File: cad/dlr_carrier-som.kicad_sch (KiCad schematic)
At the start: 5 parts, among them J5 CM4_J2

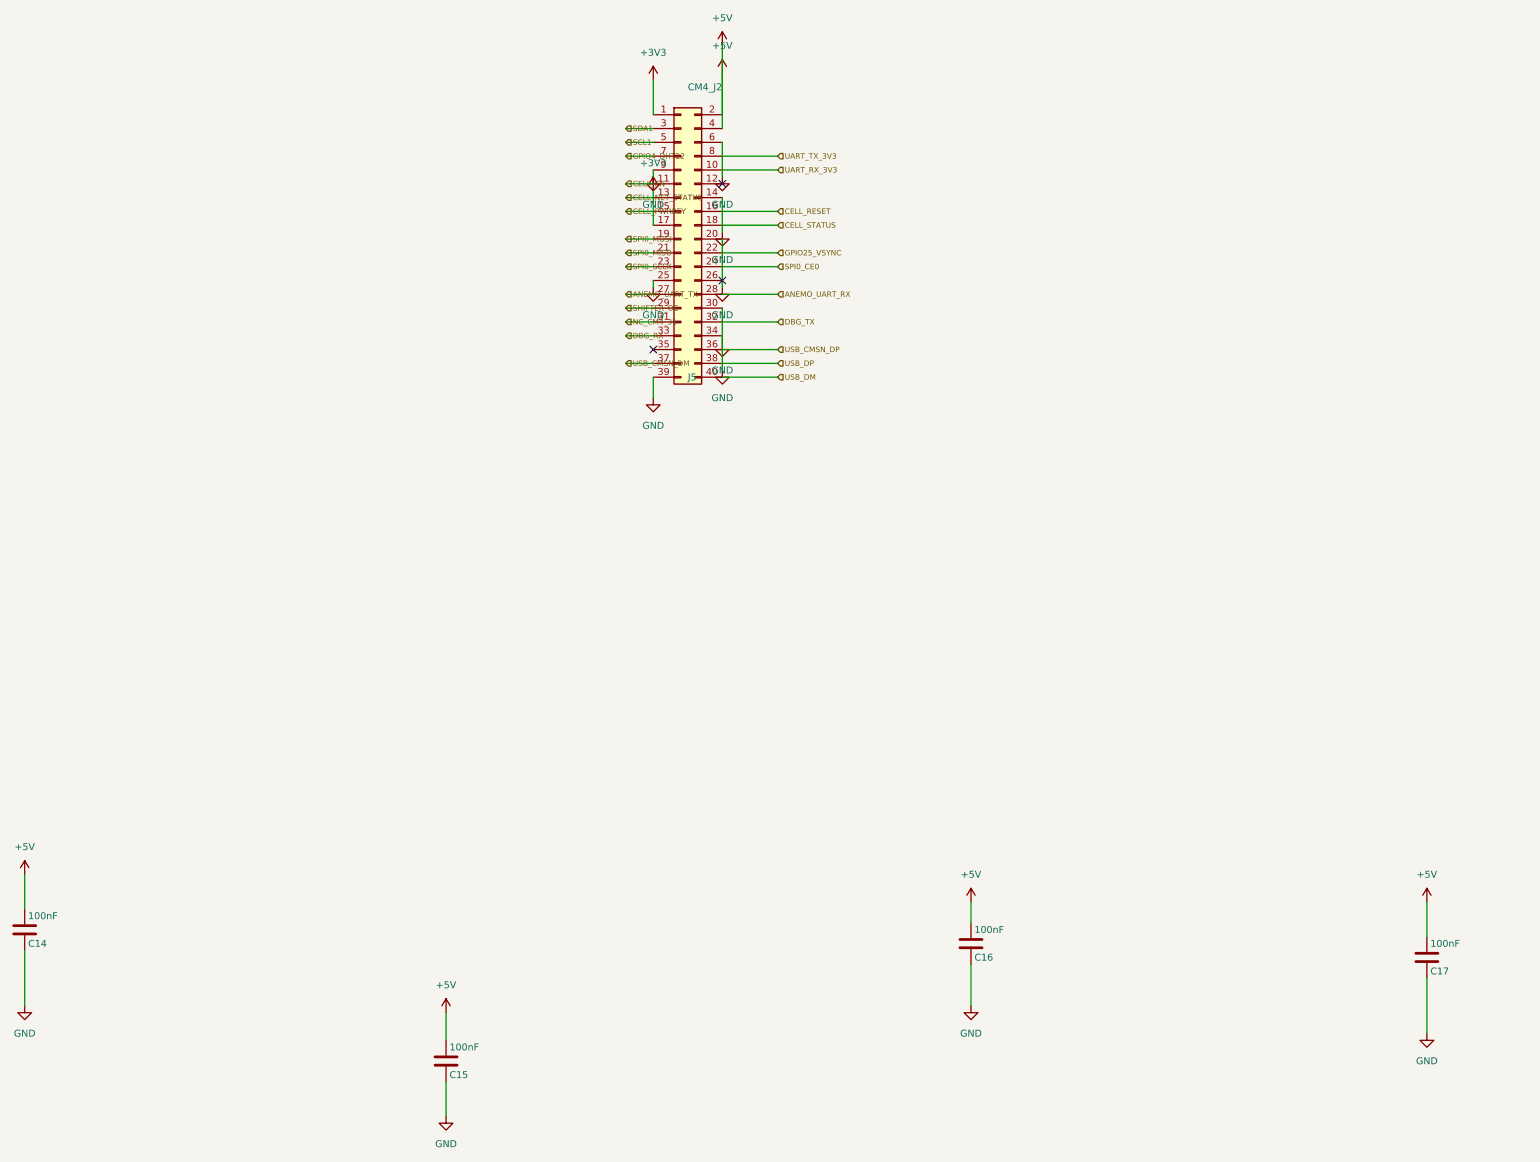
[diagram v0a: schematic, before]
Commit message: 🗺 feat(cad): scripted schematic + board pipeline, 4-layer stack
The committed board had almost every pad on +3V3 — no 5V_RAIL, VBAT or SDA1 net
existed on it at all — so the gerbers in output/ were never a valid board. Cause:
"Update PCB from Schematic" is GUI-only, so nothing kept the board honest, and the
schematic generator itself was merging nets.

Schematic generator:
  * power stubs now run along the pin direction; they used to be forced up or down
    regardless, which drove a 5V_RAIL stub straight through the buck inductor's
    BUCK_SW pin
  * PWR_FLAGs are placed by rule — any net that reaches a power-input pin with no
    power-output pin gets exactly one — instead of a hardcoded list, which is what
    the new VBAT and CHG_VCC rails needed
  * placement is deterministic; it used Python's salted hash(), so no two runs
    produced the same schematic
  * sch_guard fails the build on any cross-net wire/pin collision
  * ~700 lines of dead single-sheet generator removed
  ERC: 0 violations across all 8 sheets.

Board pipeline (cad/drawing/, all scripted, no GUI step):
  sync_pcb      rebuilds every footprint from the library and reassigns every pad
                net from the SKiDL netlist — the replacement for F8
  board_setup   4-layer SIG/GND/5V/SIG stack, rules, net classes, planes (ADR-016)
  route_pcb     DSN -> Freerouting -> SES, after patching the DSN so plane layers
                are "power" (the router was slicing the planes with signals) and
                the plane declarations are dropped (the router had been leaving
                GND and 5V pads with no path to the plane at all)
  stitch_planes vias from surface pads into their plane
  close_gaps    closes what the router leaves, using real segment-to-segment
                clearance; it never forces copper through another net

DRC: 265 unconnected -> 5, with no clearance, short, annular-ring or courtyard
errors. The remaining 5 are escapes on the DF40, the VQFN and the MSOP; they are
l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
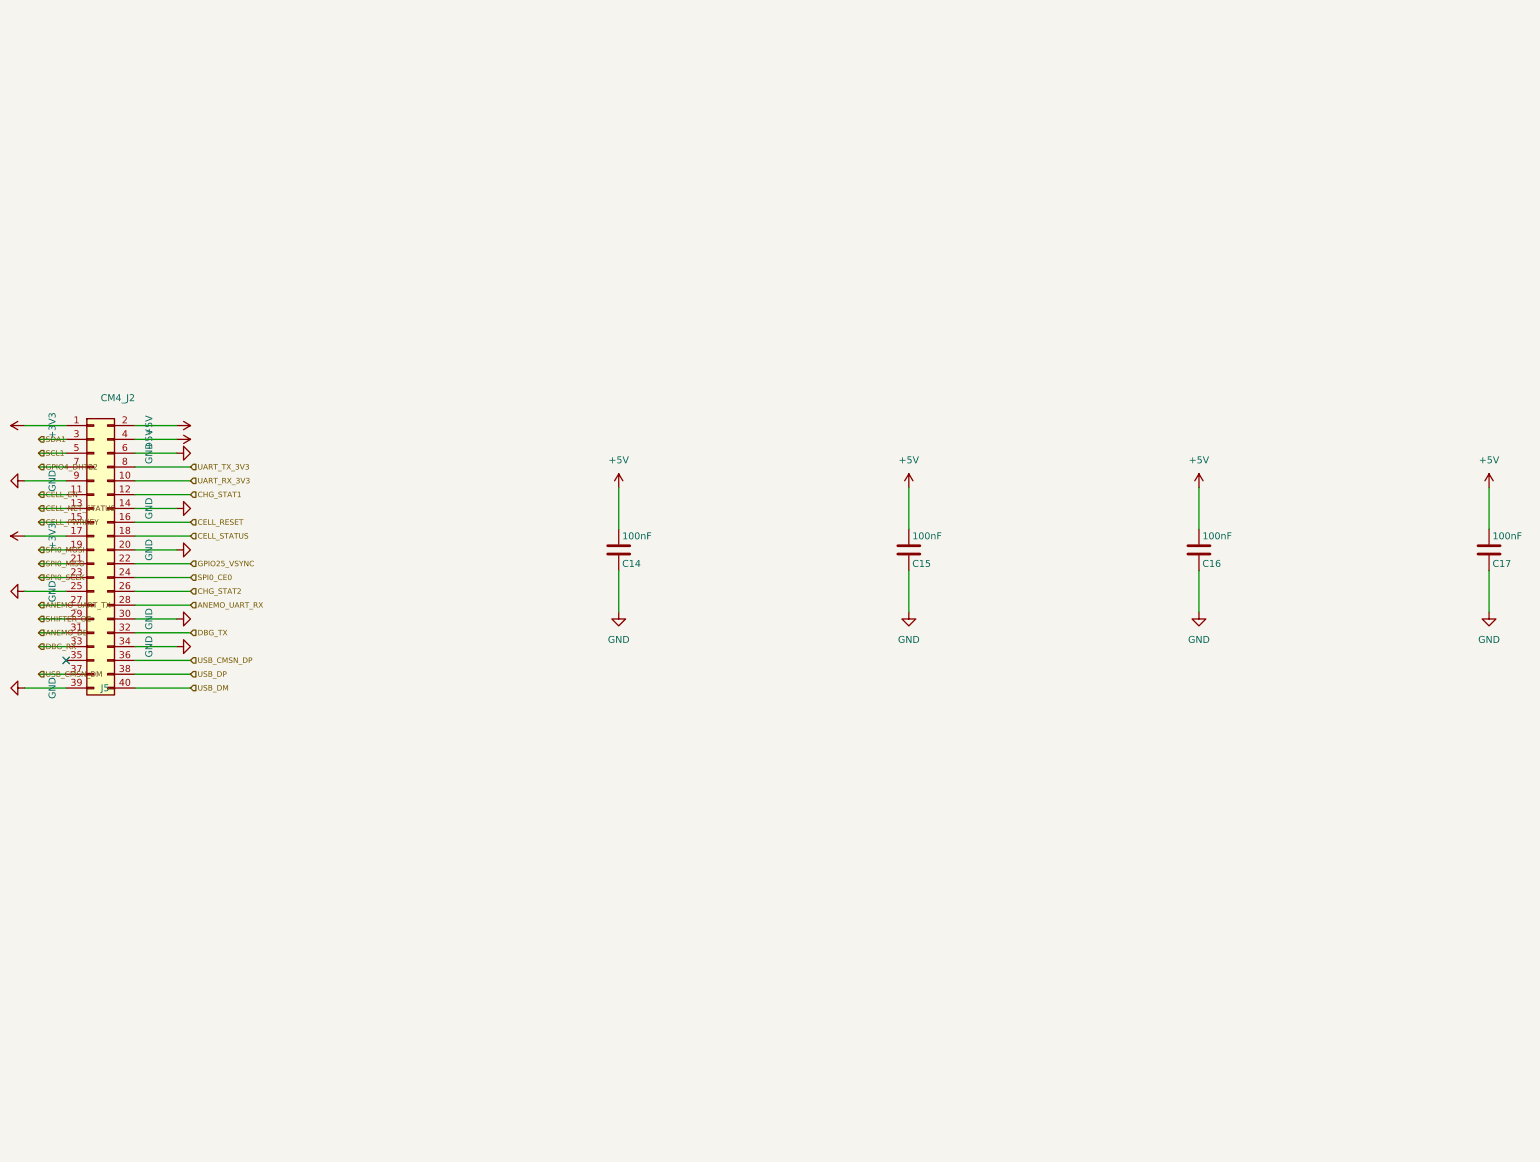
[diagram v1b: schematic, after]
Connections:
- net CHG_STAT1: now reaches J5.12 (Pin_12)
- net CHG_STAT2: now reaches J5.26 (Pin_26)
- net NC_CM4_31 renamed ANEMO_DE
- no-connect marks 3 -> 1

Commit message: 🩺 fix(schematic): match hierarchical label type to the sheet pin
The 117 KiCad 9 errors were a type mismatch, not the hierarchy metadata: every
child hierarchical label was written as `(shape input)` while the root's sheet pins
are bidirectional. KiCad's hier_label_mismatch check compares electrical type as
well as name, so on KiCad 9 every cross-sheet net failed, and the root labels then
read as dangling. KiCad 10 tolerates the mismatch, which is why it passed here.

kicad-sch-api 0.5.6 accepts a shape argument on add_hierarchical_label and ignores
it — the third serialization bug worked around in this generator — so the shape is
rewritten in the saved sheet.

Co-Authored-By: Claude Opus 5 <noreply@anthropic.com>
Claude-Session: https://claude.ai/code/session_011xr7VCL7rkJj2WE2uQF7sF
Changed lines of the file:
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@@
 		(instances
 			(project "CM4 SoM"
-				(path "/89720a6f-8597-4309-a3bf-d36a1edd93d6"
+				(path "/8bad8029-d445-45ba-bfa9-ecca933e2f0a"
 					(reference "J5")
 					(unit 1)
@@
 		(instances
 			(project "CM4 SoM"
-				(path "/89720a6f-8597-4309-a3bf-d36a1edd93d6"
+				(path "/8bad8029-d445-45ba-bfa9-ecca933e2f0a"
 					(reference "C14")
 					(unit 1)
@@
 		(instances
 			(project "CM4 SoM"
-				(path "/89720a6f-8597-4309-a3bf-d36a1edd93d6"
+				(path "/8bad8029-d445-45ba-bfa9-ecca933e2f0a"
 					(reference "C15")
 					(unit 1)
@@
 		(instances
 			(project "CM4 SoM"
-				(path "/89720a6f-8597-4309-a3bf-d36a1edd93d6"
+				(path "/8bad8029-d445-45ba-bfa9-ecca933e2f0a"
 					(reference "C16")
 					(unit 1)
@@
 		(instances
 			(project "CM4 SoM"
-				(path "/89720a6f-8597-4309-a3bf-d36a1edd93d6"
+				(path "/8bad8029-d445-45ba-bfa9-ecca933e2f0a"
 					(reference "C17")
 					(unit 1)
@@
 		(instances
 			(project "CM4 SoM"
-				(path "/89720a6f-8597-4309-a3bf-d36a1edd93d6"
+				(path "/8bad8029-d445-45ba-bfa9-ecca933e2f0a"
 					(reference "#PWR001")
 					(unit 1)
@@
 		(instances
 			(project "CM4 SoM"
-				(path "/89720a6f-8597-4309-a3bf-d36a1edd93d6"
+				(path "/8bad8029-d445-45ba-bfa9-ecca933e2f0a"
 					(reference "#PWR002")
 					(unit 1)
@@
 		(instances
 			(project "CM4 SoM"
-				(path "/89720a6f-8597-4309-a3bf-d36a1edd93d6"
+				(path "/8bad8029-d445-45ba-bfa9-ecca933e2f0a"
 					(reference "#PWR003")
 					(unit 1)
@@
 		(instances
 			(project "CM4 SoM"
-				(path "/89720a6f-8597-4309-a3bf-d36a1edd93d6"
+				(path "/8bad8029-d445-45ba-bfa9-ecca933e2f0a"
 					(reference "#PWR004")
 					(unit 1)
@@
 		(instances
 			(project "CM4 SoM"
-				(path "/89720a6f-8597-4309-a3bf-d36a1edd93d6"
+				(path "/8bad8029-d445-45ba-bfa9-ecca933e2f0a"
 					(reference "#PWR005")
 					(unit 1)
@@
 		(instances
 			(project "CM4 SoM"
-				(path "/89720a6f-8597-4309-a3bf-d36a1edd93d6"
+				(path "/8bad8029-d445-45ba-bfa9-ecca933e2f0a"
 					(reference "#PWR006")
 					(unit 1)
@@
 		(instances
 			(project "CM4 SoM"
-				(path "/89720a6f-8597-4309-a3bf-d36a1edd93d6"
+				(path "/8bad8029-d445-45ba-bfa9-ecca933e2f0a"
 					(reference "#PWR007")
 					(unit 1)
@@
 		(instances
 			(project "CM4 SoM"
-				(path "/89720a6f-8597-4309-a3bf-d36a1edd93d6"
+				(path "/8bad8029-d445-45ba-bfa9-ecca933e2f0a"
 					(reference "#PWR008")
 					(unit 1)
@@
 		(instances
 			(project "CM4 SoM"
-				(path "/89720a6f-8597-4309-a3bf-d36a1edd93d6"
+				(path "/8bad8029-d445-45ba-bfa9-ecca933e2f0a"
 					(reference "#PWR009")
 					(unit 1)
@@
 		(instances
 			(project "CM4 SoM"
-				(path "/89720a6f-8597-4309-a3bf-d36a1edd93d6"
+				(path "/8bad8029-d445-45ba-bfa9-ecca933e2f0a"
 					(reference "#PWR010")
 					(unit 1)
@@
 		(instances
 			(project "CM4 SoM"
-				(path "/89720a6f-8597-4309-a3bf-d36a1edd93d6"
+				(path "/8bad8029-d445-45ba-bfa9-ecca933e2f0a"
 					(reference "#PWR011")
 					(unit 1)
@@
 		(instances
 			(project "CM4 SoM"
-				(path "/89720a6f-8597-4309-a3bf-d36a1edd93d6"
+				(path "/8bad8029-d445-45ba-bfa9-ecca933e2f0a"
 					(reference "#PWR012")
 					(unit 1)
@@
 		(instances
 			(project "CM4 SoM"
-				(path "/89720a6f-8597-4309-a3bf-d36a1edd93d6"
+				(path "/8bad8029-d445-45ba-bfa9-ecca933e2f0a"
 					(reference "#PWR013")
 					(unit 1)
@@
 		(instances
 			(project "CM4 SoM"
-				(path "/89720a6f-8597-4309-a3bf-d36a1edd93d6"
+				(path "/8bad8029-d445-45ba-bfa9-ecca933e2f0a"
 					(reference "#PWR014")
 					(unit 1)
@@
 		(instances
 			(project "CM4 SoM"
-				(path "/89720a6f-8597-4309-a3bf-d36a1edd93d6"
+				(path "/8bad8029-d445-45ba-bfa9-ecca933e2f0a"
 					(reference "#PWR015")
 					(unit 1)
@@
 		(instances
 			(project "CM4 SoM"
-				(path "/89720a6f-8597-4309-a3bf-d36a1edd93d6"
+				(path "/8bad8029-d445-45ba-bfa9-ecca933e2f0a"
 					(reference "#PWR016")
 					(unit 1)
@@
 		(instances
 			(project "CM4 SoM"
-				(path "/89720a6f-8597-4309-a3bf-d36a1edd93d6"
+				(path "/8bad8029-d445-45ba-bfa9-ecca933e2f0a"
 					(reference "#PWR017")
 					(unit 1)
@@
 		(instances
 			(project "CM4 SoM"
-				(path "/89720a6f-8597-4309-a3bf-d36a1edd93d6"
+				(path "/8bad8029-d445-45ba-bfa9-ecca933e2f0a"
 					(reference "#PWR018")
 					(unit 1)
@@
 		(instances
 			(project "CM4 SoM"
-				(path "/89720a6f-8597-4309-a3bf-d36a1edd93d6"
+				(path "/8bad8029-d445-45ba-bfa9-ecca933e2f0a"
 					(reference "#PWR019")
 					(unit 1)
@@
 		(instances
 			(project "CM4 SoM"
-				(path "/89720a6f-8597-4309-a3bf-d36a1edd93d6"
+				(path "/8bad8029-d445-45ba-bfa9-ecca933e2f0a"
 					(reference "#PWR020")
 					(unit 1)
@@
 	)
 	(hierarchical_label "ANEMO_DE"
-		(shape input)
+		(shape bidirectional)
 		(at 97.79 180.34 180)
 		(effects
@@
 	)
 	(hierarchical_label "ANEMO_UART_RX"
-		(shape input)
+		(shape bidirectional)
 		(at 125.73 175.26 0)
 		(effects
@@
 	)
 	(hierarchical_label "ANEMO_UART_TX"
-		(shape input)
+		(shape bidirectional)
 		(at 97.79 175.26 180)
 		(effects
@@
 	)
 	(hierarchical_label "CELL_EN"
-		(shape input)
+		(shape bidirectional)
 		(at 97.79 154.94 180)
 		(effects
@@
 	)
 	(hierarchical_label "CELL_NET_STATUS"
-		(shape input)
+		(shape bidirectional)
 		(at 97.79 157.48 180)
 		(effects
@@
 	)
 	(hierarchical_label "CELL_PWRKEY"
-		(shape input)
+		(shape bidirectional)
 		(at 97.79 160.02 180)
 		(effects
@@
 	)
 	(hierarchical_label "CELL_RESET"
-		(shape input)
+		(shape bidirectional)
 		(at 125.73 160.02 0)
 		(effects
@@
 	)
 	(hierarchical_label "CELL_STATUS"
-		(shape input)
+		(shape bidirectional)
 		(at 125.73 162.56 0)
 		(effects
@@
 	)
 	(hierarchical_label "CHG_STAT1"
-		(shape input)
+		(shape bidirectional)
 		(at 125.73 154.94 0)
 		(effects
@@
 	)
 	(hierarchical_label "CHG_STAT2"
-		(shape input)
+		(shape bidirectional)
 		(at 125.73 172.72 0)
 		(effects
@@
 	)
 	(hierarchical_label "DBG_RX"
-		(shape input)
+		(shape bidirectional)
 		(at 97.79 182.88 180)
 		(effects
@@
 	)
 	(hierarchical_label "DBG_TX"
-		(shape input)
+		(shape bidirectional)
 		(at 125.73 180.34 0)
 		(effects
@@
 	)
 	(hierarchical_label "GPIO25_VSYNC"
-		(shape input)
+		(shape bidirectional)
 		(at 125.73 167.64 0)
 		(effects
@@
 	)
 	(hierarchical_label "GPIO4_DHT22"
-		(shape input)
+		(shape bidirectional)
 		(at 97.79 149.86 180)
 		(effects
@@
 	)
 	(hierarchical_label "SCL1"
-		(shape input)
+		(shape bidirectional)
 		(at 97.79 147.32 180)
 		(effects
@@
 	)
 	(hierarchical_label "SDA1"
-		(shape input)
+		(shape bidirectional)
 		(at 97.79 144.78 180)
 		(effects
@@
 	)
 	(hierarchical_label "SHIFTER_OE"
-		(shape input)
+		(shape bidirectional)
 		(at 97.79 177.8 180)
 		(effects
@@
 	)
 	(hierarchical_label "SPI0_CE0"
-		(shape input)
+		(shape bidirectional)
 		(at 125.73 170.18 0)
 		(effects
@@
 	)
 	(hierarchical_label "SPI0_MISO"
-		(shape input)
+		(shape bidirectional)
 		(at 97.79 167.64 180)
 		(effects
@@
 	)
 	(hierarchical_label "SPI0_MOSI"
-		(shape input)
+		(shape bidirectional)
 		(at 97.79 165.1 180)
 		(effects
@@
 	)
 	(hierarchical_label "SPI0_SCLK"
-		(shape input)
+		(shape bidirectional)
 		(at 97.79 170.18 180)
 		(effects
@@
 	)
 	(hierarchical_label "UART_RX_3V3"
-		(shape input)
+		(shape bidirectional)
 		(at 125.73 152.4 0)
 		(effects
@@
 	)
 	(hierarchical_label "UART_TX_3V3"
-		(shape input)
+		(shape bidirectional)
 		(at 125.73 149.86 0)
 		(effects
@@
 	)
 	(hierarchical_label "USB_CMSN_DM"
-		(shape input)
+		(shape bidirectional)
 		(at 97.79 187.96 180)
 		(effects
@@
 	)
 	(hierarchical_label "USB_CMSN_DP"
-		(shape input)
+		(shape bidirectional)
 		(at 125.73 185.42 0)
 		(effects
@@
 	)
 	(hierarchical_label "USB_DM"
-		(shape input)
+		(shape bidirectional)
 		(at 125.73 190.5 0)
 		(effects
@@
 	)
 	(hierarchical_label "USB_DP"
-		(shape input)
+		(shape bidirectional)
 		(at 125.73 187.96 0)
 		(effects
@@
 	)
 	(sheet_instances
-		(path "/fb0d3d2e-7f02-4ddc-9d16-9e0020fdfa07"
+		(path "/4a3e06bc-d7fd-4803-a708-54e05d93e811"
 			(page "4")
 		)
